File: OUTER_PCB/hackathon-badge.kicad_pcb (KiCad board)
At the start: 2 copper layers, 97.8 x 87.5 mm, 20 parts

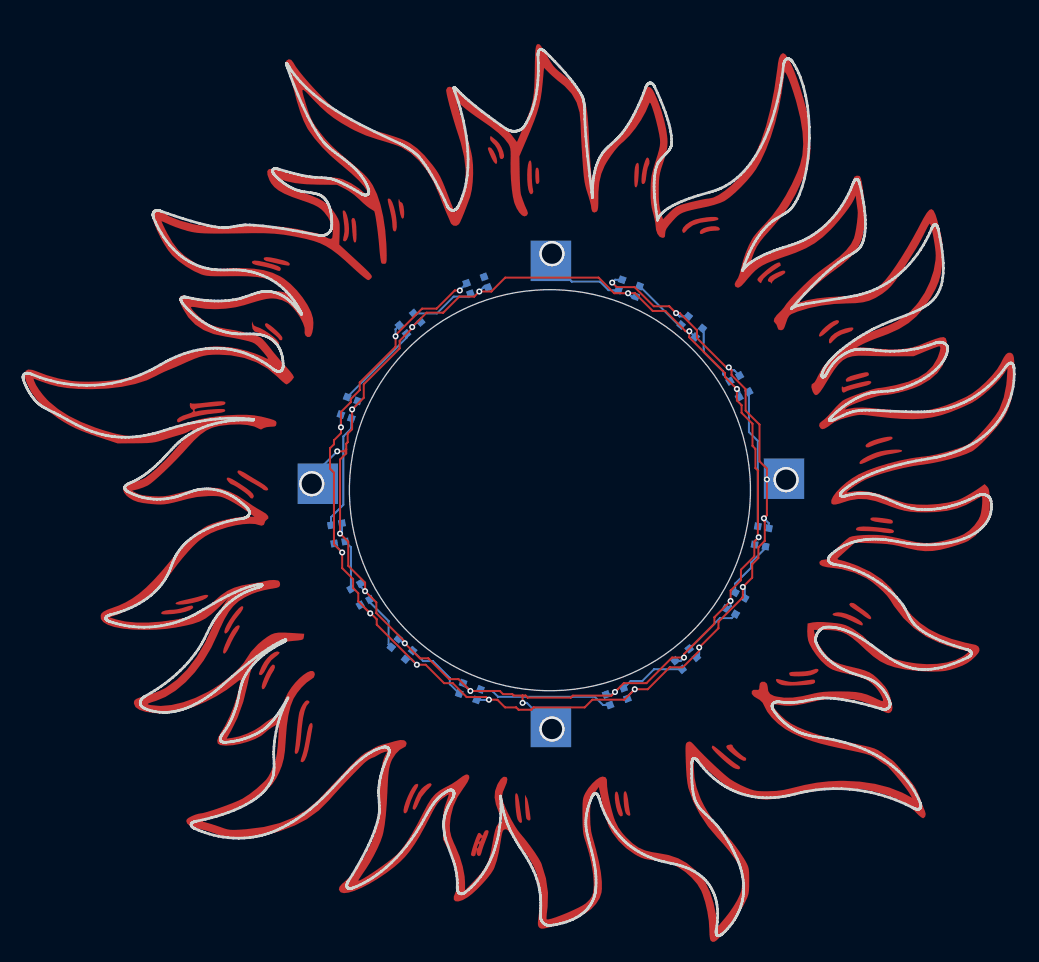
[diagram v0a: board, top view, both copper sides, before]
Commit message: modifying the external part of the badge so that JLC doesn't get mad at me
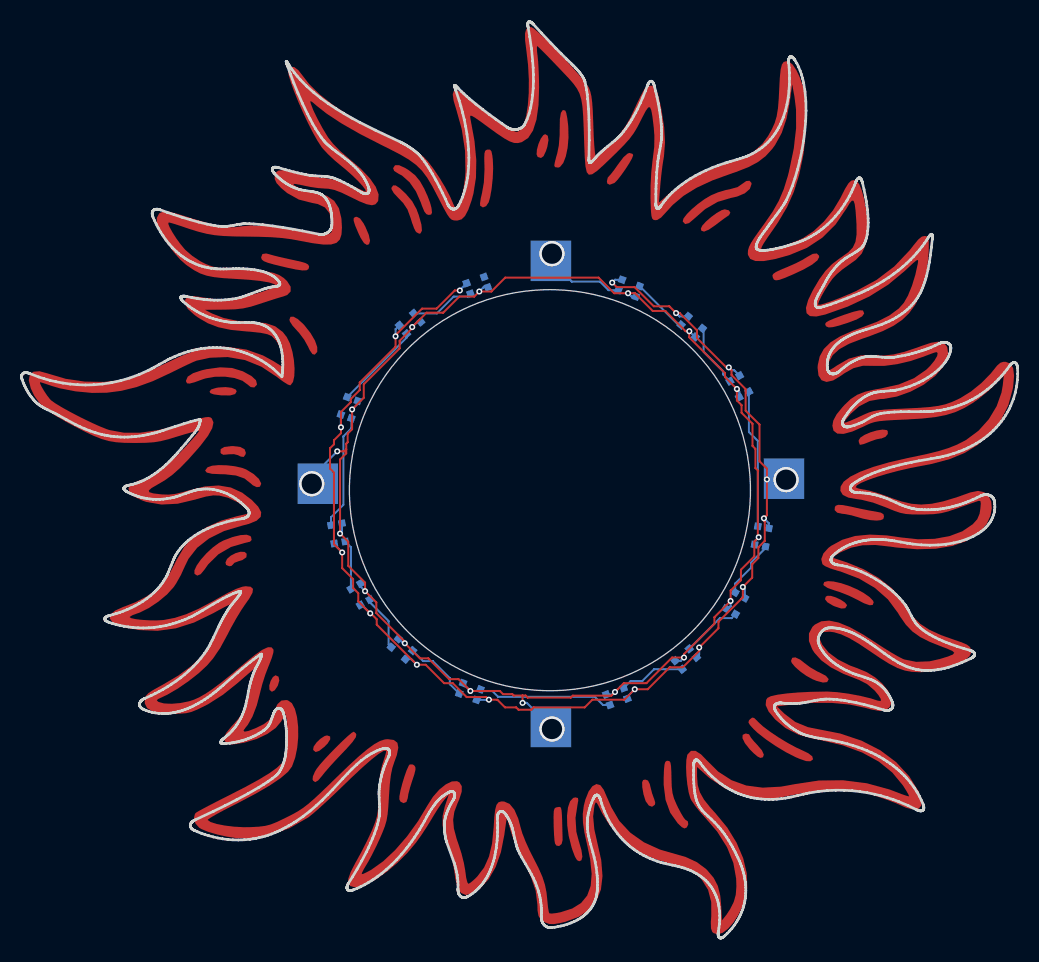
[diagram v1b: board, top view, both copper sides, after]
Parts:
- moved G*** 0.09 mm to (150.9, 107.1)
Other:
- board size 97.8 x 87.5 mm -> 98.3 x 90.4 mm
